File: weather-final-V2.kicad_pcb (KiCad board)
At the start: 4 copper layers, 45 x 60 mm, 41 parts, among them J1 Conn_02x04_Odd_Even, J2 Conn_01x06_Pin, J3 PROGRAMMING_CONN, J4 USB_C_Receptacle_PowerOnly_6P, U1 AMS1117-5.0, U2 ATmega328-P, Y1 Crystal

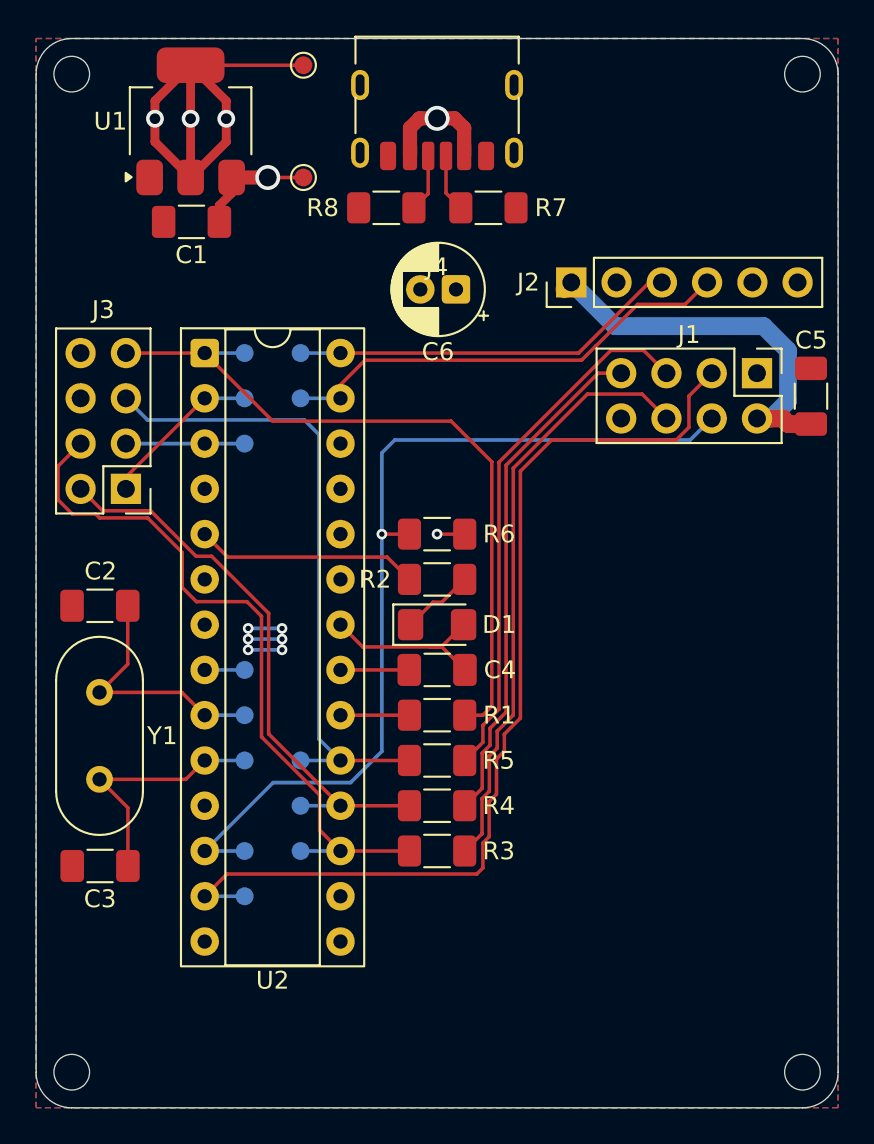
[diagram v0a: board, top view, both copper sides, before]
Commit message: Add 2 more layers to PCB - 3V3 and GND. Route some signal traces in 3rd layer to get continuous GND plane on top and 5V plane in bottom. Remove unnecessary traces.
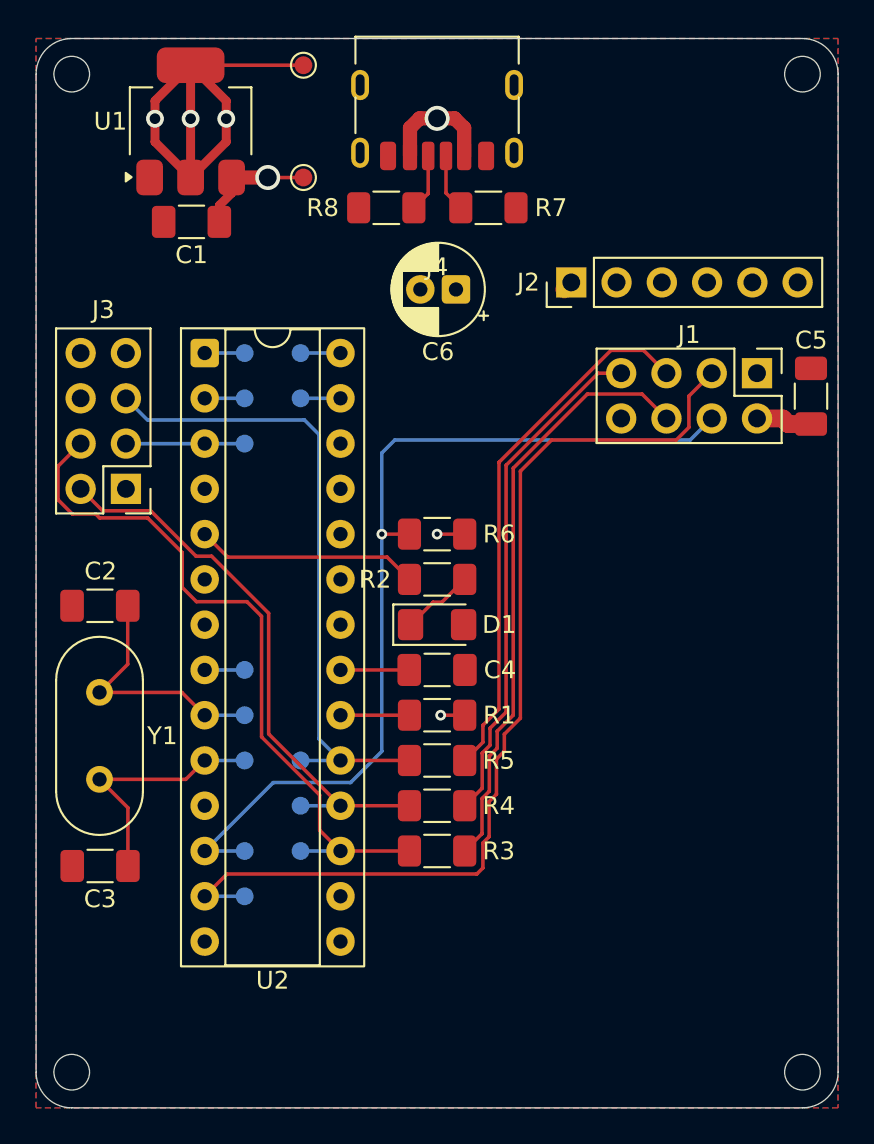
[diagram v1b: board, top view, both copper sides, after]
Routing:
- net +3V3: track 51.0 -> 32.3 mm
- net GND: track 18.4 -> 2.24 mm, vias 6 -> 0
- net RESET: track 40.7 -> 42.0 mm, vias 0 -> 1

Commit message: Add i2c pullups Clean unnecessary trace widths Add diode for reverse voltage protection on J3 input
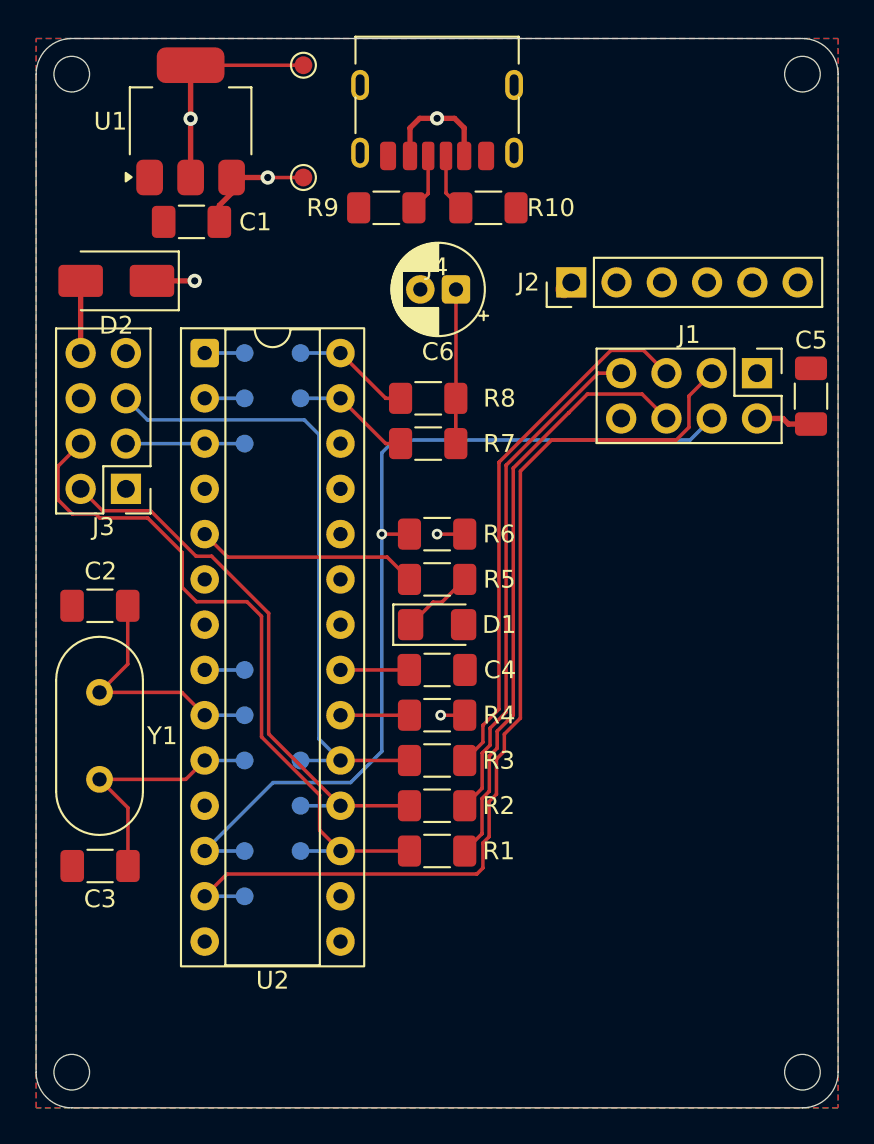
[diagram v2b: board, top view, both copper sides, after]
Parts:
- added D2: US1A, Diode_SMD:D_SMA, F.Cu at (4.50, 13.6)
- added R7: R, Resistor_SMD:R_1206_3216Metric_Pad1.30x1.75mm_HandSolder, F.Cu at (22.0, 22.7)
- added R8: R, Resistor_SMD:R_1206_3216Metric_Pad1.30x1.75mm_HandSolder, F.Cu at (22.0, 20.2)
- renumbered R3 to R1, R7 to R10, R4 to R2, R5 to R3, R1 to R4, R2 to R5, R8 to R9
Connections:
- J3 pad 8: +5V -> Net-(D2-A)
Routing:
- net +3V3: track 32.3 -> 25.0 mm, vias 3 -> 1
- net SCL: track 21.9 -> 26.3 mm
- net SDA: track 25.5 -> 29.9 mm
- net Net-(D2-A): track 0.00 -> 4.05 mm
- net +5V: track 18.9 -> 21.3 mm, vias 3 -> 4

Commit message: Edit silkscreen width and positions
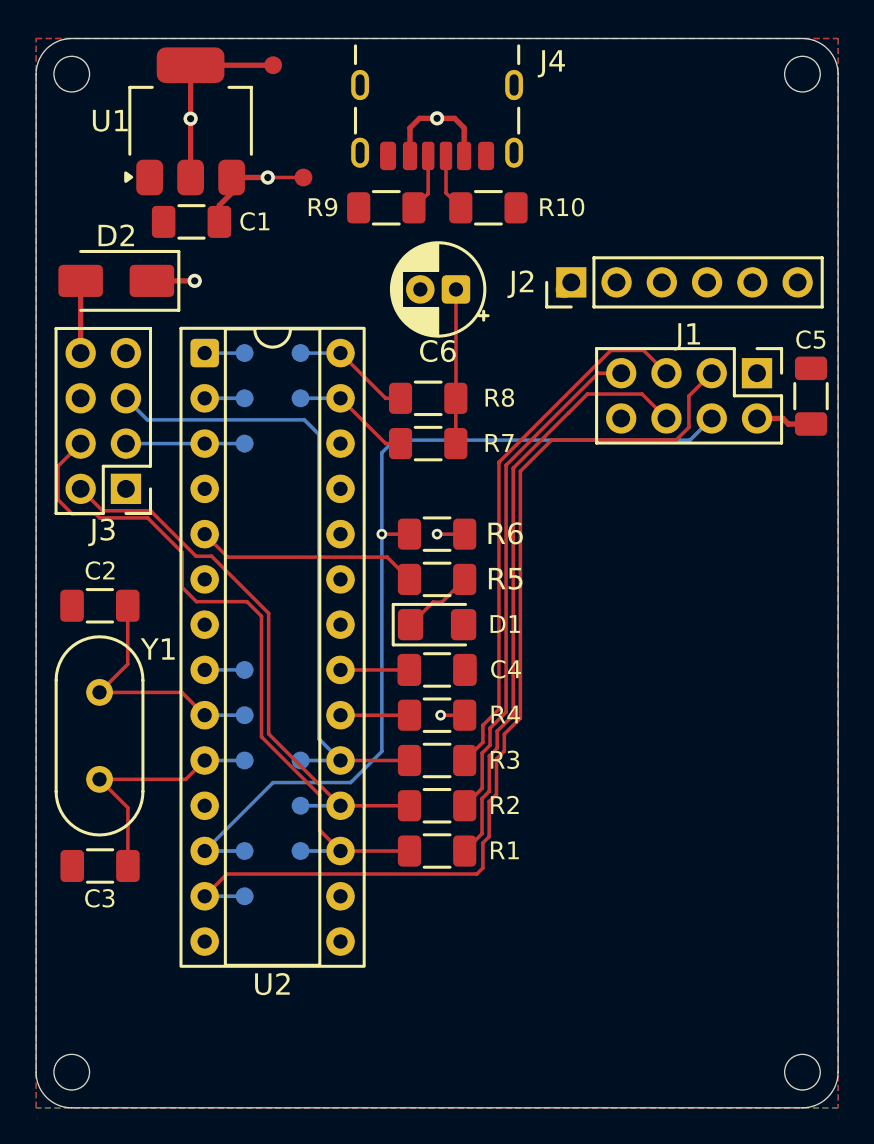
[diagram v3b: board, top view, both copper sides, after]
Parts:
- moved TP11 1.70 mm to (13.3, 1.50)
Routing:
- net +3V3: track 25.0 -> 23.3 mm

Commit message: Add stitching vias
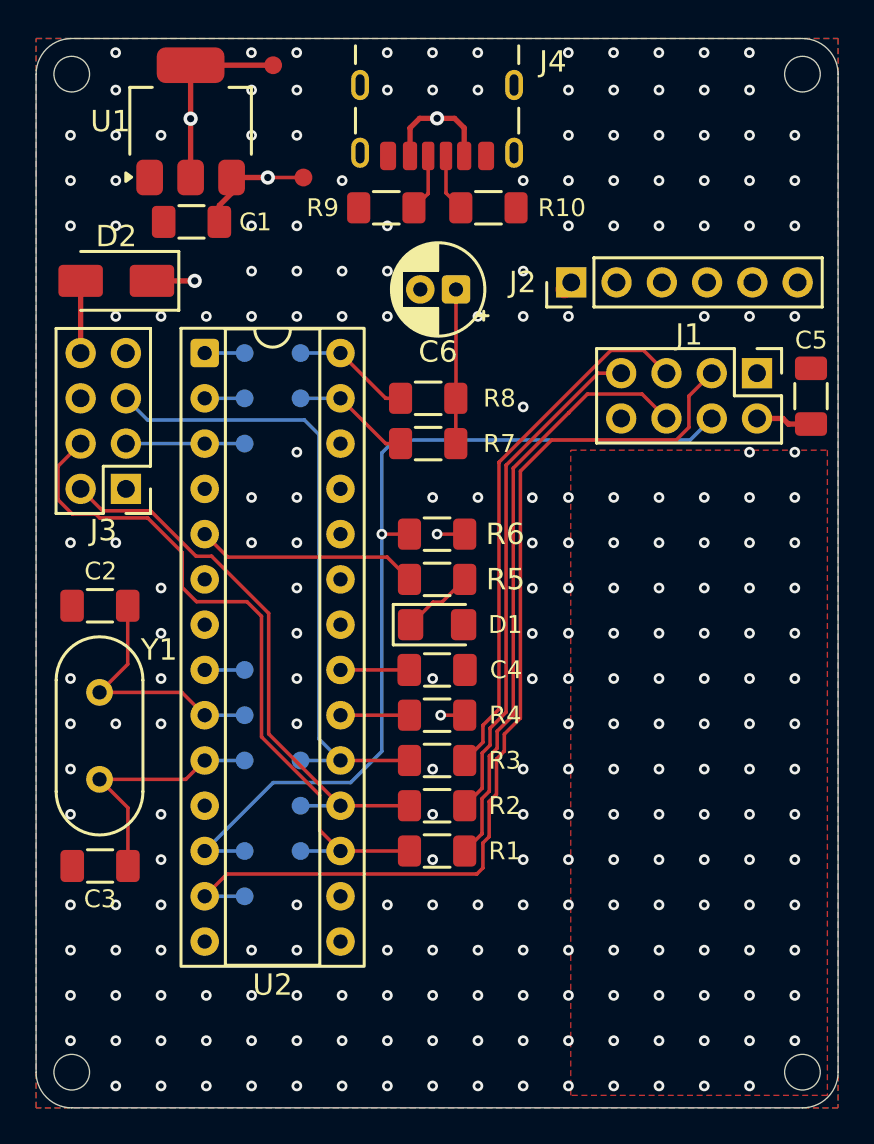
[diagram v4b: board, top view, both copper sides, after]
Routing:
- net GND: vias 0 -> 244

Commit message: Add board-edge stitching vias
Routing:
- net GND: vias 244 -> 274

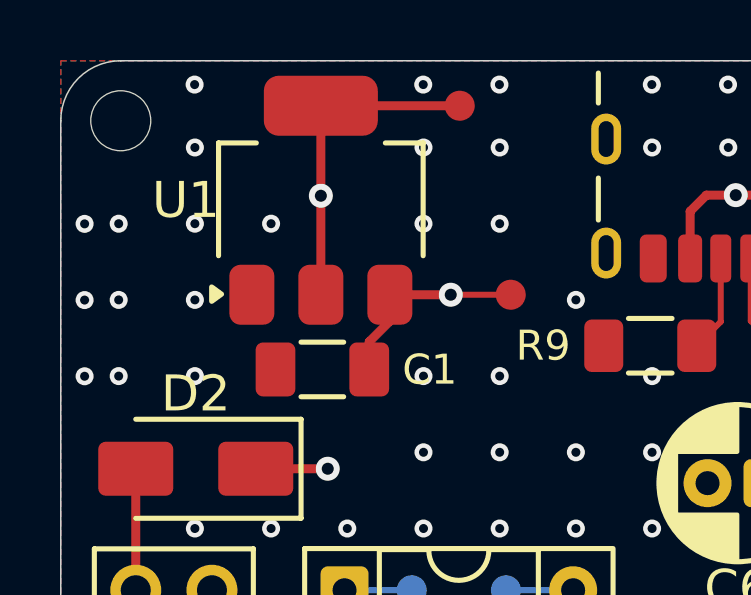
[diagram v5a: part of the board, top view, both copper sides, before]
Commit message: Add i2c pullup resistors' values Fix a silkscreen overlap
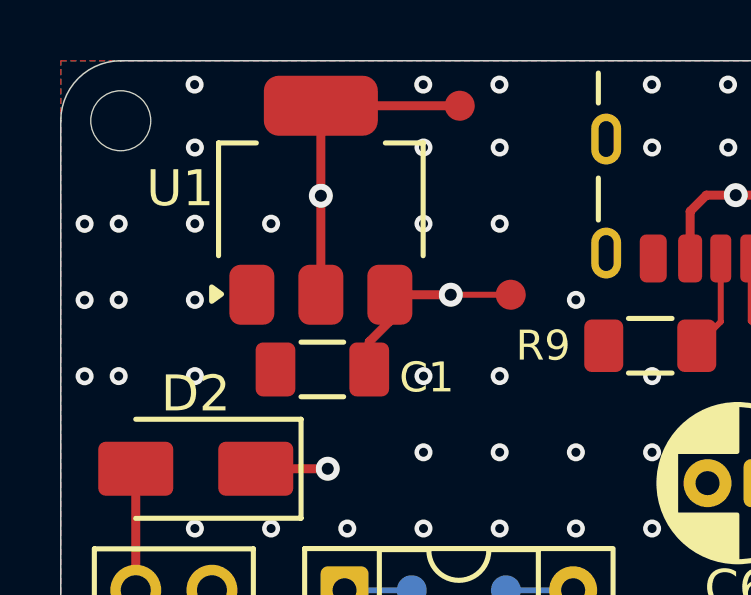
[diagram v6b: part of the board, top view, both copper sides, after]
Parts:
- R7, R8: value R -> 4.7K
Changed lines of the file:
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@@
 			)
 		)
-		(property "Value" "R"
+		(property "Value" "4.7K"
 			(at 0 1.83 0)
 			(layer "F.Fab")
@@
 			)
 		)
-		(property "Value" "R"
+		(property "Value" "4.7K"
 			(at 0 1.83 0)
 			(layer "F.Fab")
@@
 		(tags "capacitor handsolder")
 		(property "Reference" "C1"
-			(at -3.58 -0.01 0)
+			(at -3.48 -0.27 0)
 			(layer "F.SilkS")
 			(effects
@@
 		(tags "CMS SOT")
 		(property "Reference" "U1"
-			(at 0 -4.5 180)
+			(at 0.39 -4.69 180)
 			(layer "F.SilkS")
 			(effects

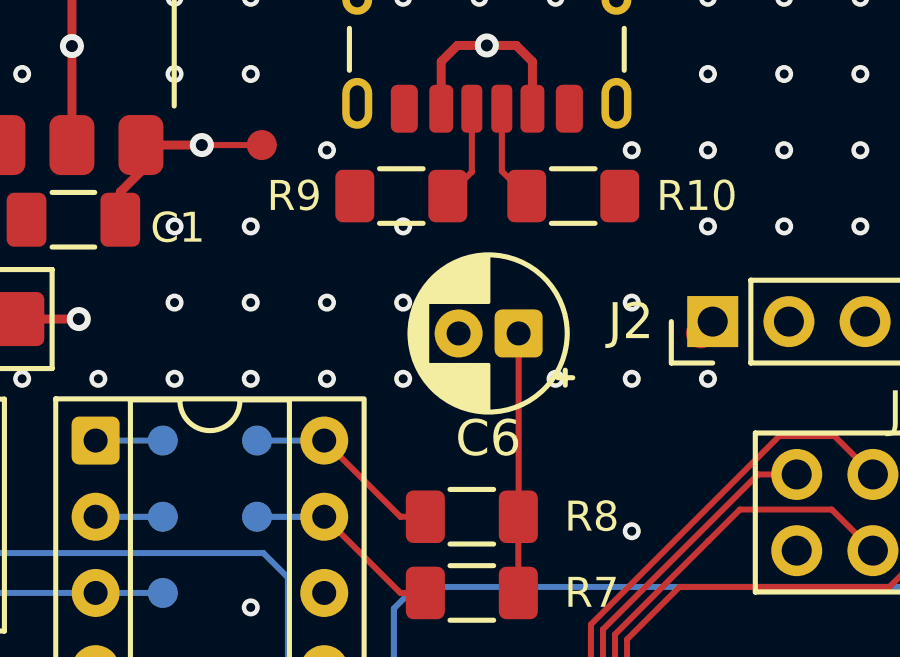
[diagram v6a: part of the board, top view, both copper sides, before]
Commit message: Add a 5V power rail decoupling capacitor Add LICENSE and README
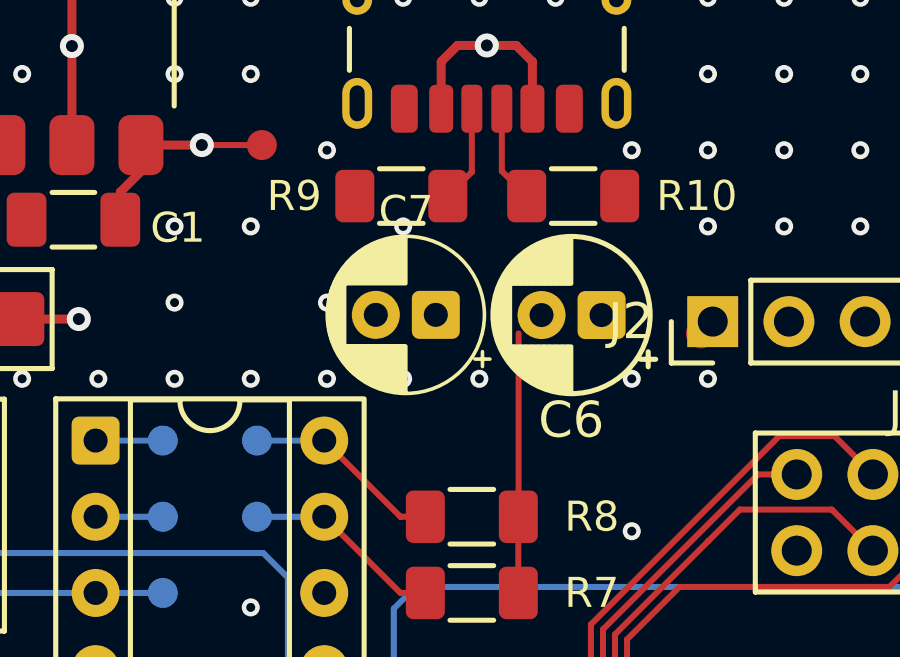
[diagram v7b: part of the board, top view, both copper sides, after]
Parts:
- added C7: 100μF, Capacitor_THT:CP_Radial_D5.0mm_P2.00mm, F.Cu at (20.8, 13.5)
- moved C6 2.83 mm to (26.3, 13.5)
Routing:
- net GND: vias 274 -> 271
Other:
- board text added: "26/04/2026"
- board text added: "ADITYA PANDURANG DESHPANDE"
- board text added: "PCB DESIGNED BY:"

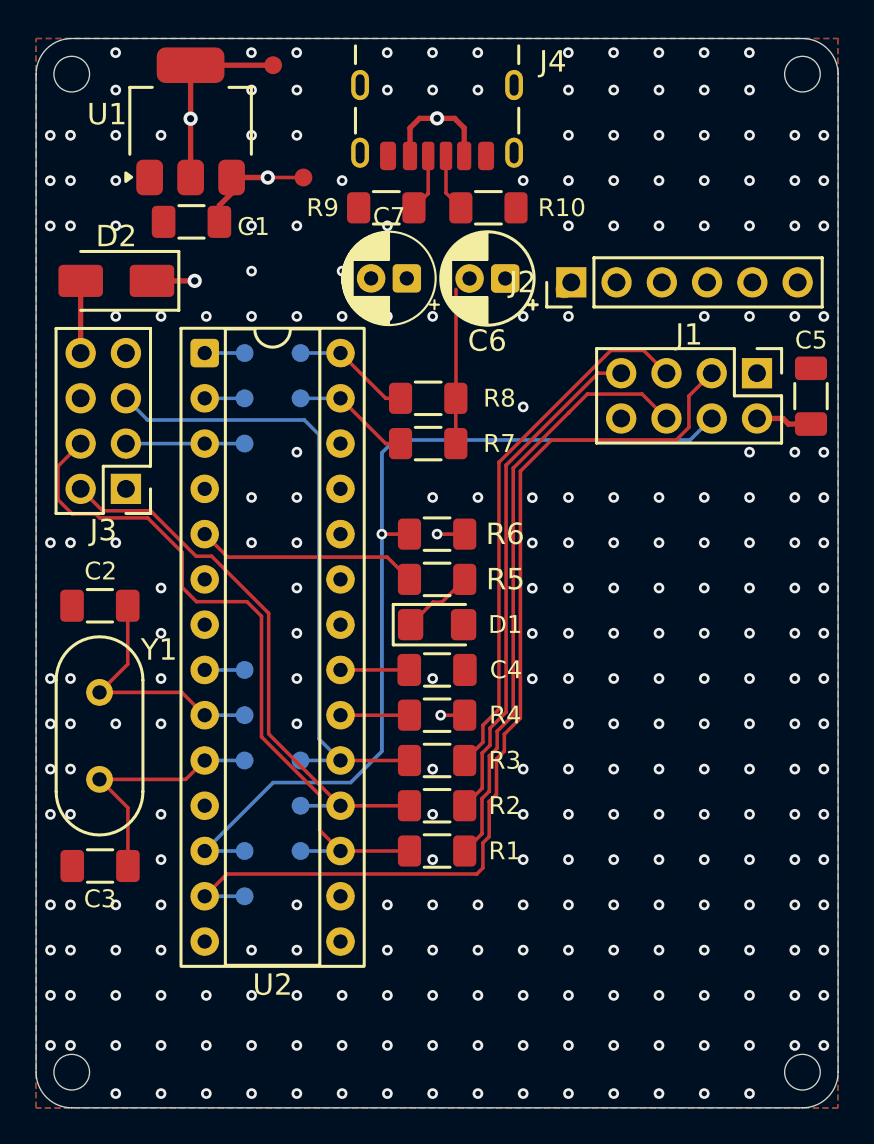
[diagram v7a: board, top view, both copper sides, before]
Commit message: Add AVCC decoupling capacitor, Change symbol of 5V to 3V3 converter from AMS1117-5.0 to AMS1117-3.3, Clean up schematics
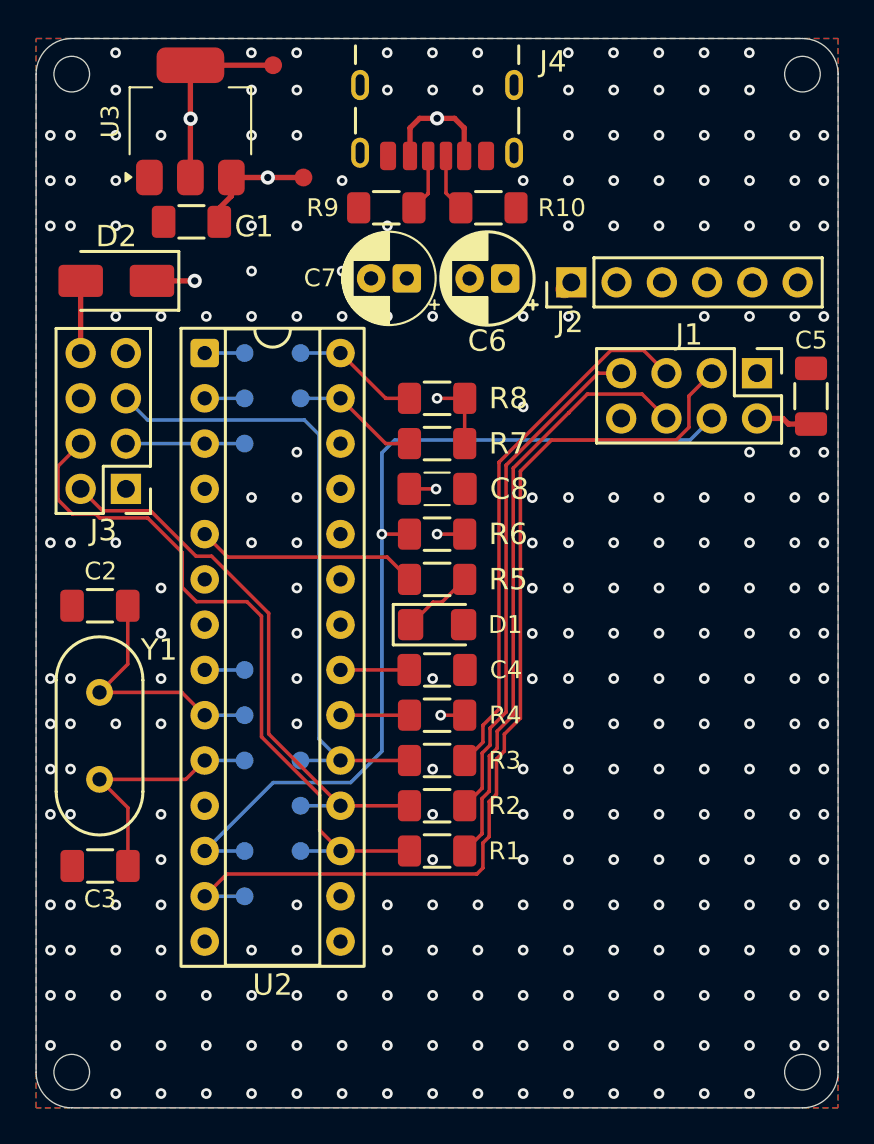
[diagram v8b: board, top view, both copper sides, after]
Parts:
- removed U1: AMS1117-5.0, Package_TO_SOT_SMD:SOT-223-3_TabPin2
- added C8: 0.1μF, Capacitor_SMD:C_1206_3216Metric_Pad1.33x1.80mm_HandSolder, F.Cu at (22.5, 25.3)
- added U3: AMS1117-3.3, Package_TO_SOT_SMD:SOT-223-3_TabPin2, F.Cu at (8.66, 4.65)
- moved R7 0.50 mm to (22.5, 22.7)
- moved R8 0.50 mm to (22.5, 20.2)
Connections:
- net Net-(U2-AREF) renamed AREF
- net Net-(U2-PD3) renamed LED
- net Net-(U2-XTAL1/PB6) renamed XTAL1
- net Net-(U2-XTAL2/PB7) renamed XTAL2
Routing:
- net +3V3: track 23.3 -> 19.5 mm, vias 1 -> 2
- net +5V: track 21.3 -> 22.8 mm, vias 4 -> 5
- net SDA: track 29.9 -> 30.4 mm
- net SCL: track 26.3 -> 26.8 mm
- net GND: vias 271 -> 268
